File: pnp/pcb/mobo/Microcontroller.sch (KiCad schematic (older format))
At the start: 31 parts

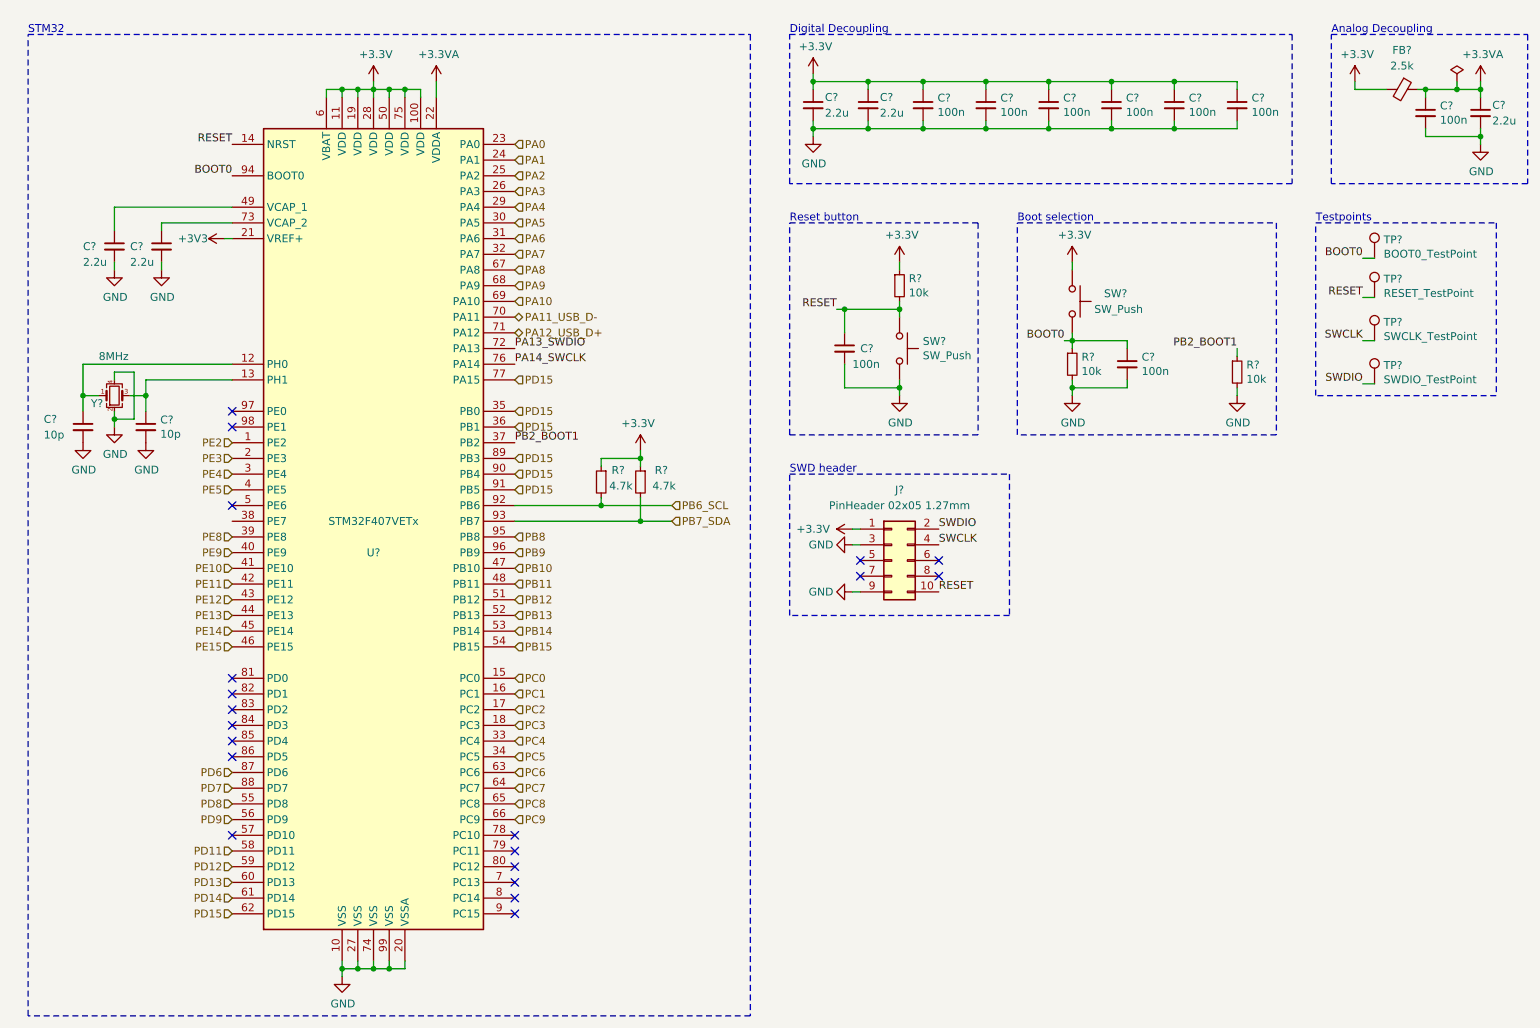
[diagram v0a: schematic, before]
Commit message: Schematic improvements
Ready for review @G-Pereira

No changes to PCB were made.

All symbol fields are not checked against the original symbols.
If wanted, an Index admin could restore this using the REV003 commit.
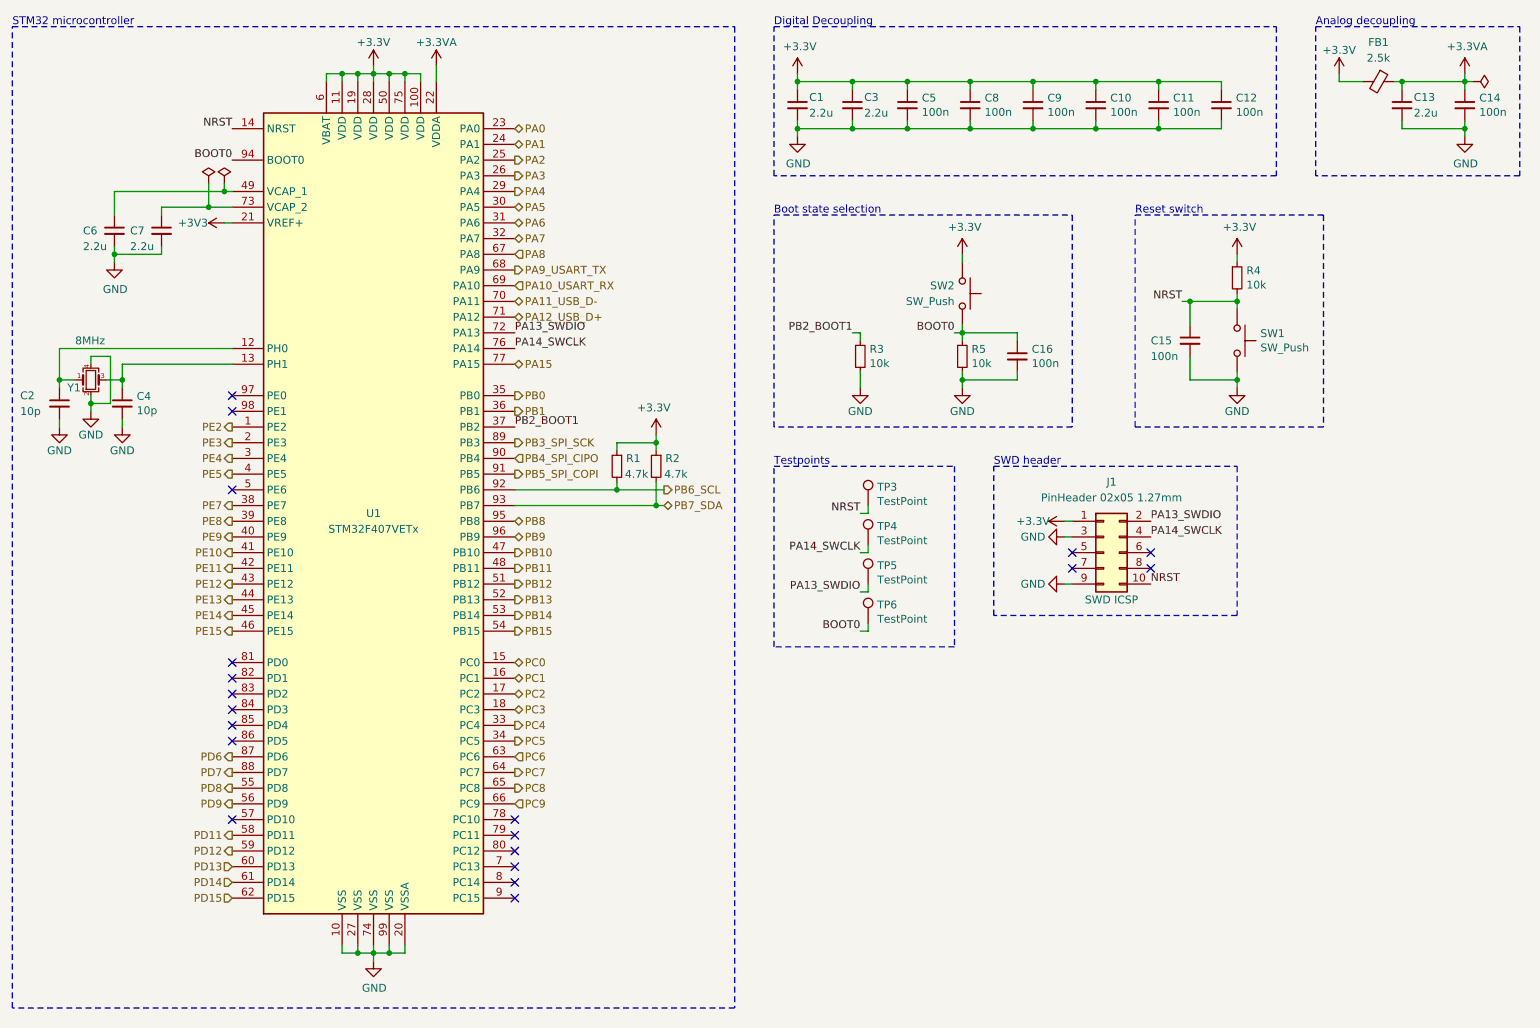
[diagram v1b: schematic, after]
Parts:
- removed C? (x2): 10p, Capacitor_SMD:C_0805_2012Metric, symbol Device:C_Small
- removed C? (x5): 2.2u, Capacitor_SMD:C_0805_2012Metric, symbol Device:C_Small
- removed C? (x9): 100n, Capacitor_SMD:C_0805_2012Metric, symbol Device:C_Small
- removed FB?: 2.5k, Inductor_SMD:L_0805_2012Metric, symbol Device:Ferrite_Bead_Small
- removed J?: PinHeader 02x05 1.27mm, symbol Connector_Generic:Conn_02x05_Odd_Even
- removed R? (x2): 4.7k, Resistor_SMD:R_0805_2012Metric, symbol Device:R_Small
- removed R? (x3): 10k, Resistor_SMD:R_0805_2012Metric, symbol Device:R_Small
- removed SW? (x2): SW_Push, Button_Switch_SMD:SW_SPST_B3S-1000, symbol Switch:SW_Push
- removed TP?: BOOT0_TestPoint, TestPoint:TestPoint_Pad_D2.0mm, symbol Connector:TestPoint
- removed TP?: RESET_TestPoint, TestPoint:TestPoint_Pad_D2.0mm, symbol Connector:TestPoint
- removed TP?: SWCLK_TestPoint, TestPoint:TestPoint_Pad_D2.0mm, symbol Connector:TestPoint
- removed TP?: SWDIO_TestPoint, TestPoint:TestPoint_Pad_D2.0mm, symbol Connector:TestPoint
- removed U?: STM32F407VETx, Package_QFP:LQFP-100_14x14mm_P0.5mm, symbol MCU_ST_STM32F4:STM32F407VETx
- removed Y?: 8MHz, Crystal:Crystal_SMD_3225-4Pin_3.2x2.5mm, symbol Device:Crystal_GND24_Small
- added C1, C13, C3, C6, C7: 2.2u, Capacitor_SMD:C_0805_2012Metric, symbol Device:C_Small
- added C10, C11, C12, C14, C15, C16, C5, C8, C9: 100n, Capacitor_SMD:C_0805_2012Metric, symbol Device:C_Small
- added C2, C4: 10p, Capacitor_SMD:C_0805_2012Metric, symbol Device:C_Small
- added FB1: 2.5k, Inductor_SMD:L_0805_2012Metric, symbol Device:Ferrite_Bead_Small
- added J1: PinHeader 02x05 1.27mm, Connector_PinHeader_1.27mm:PinHeader_2x05_P1.27mm_Vertical_SMD, symbol Connector_Generic:Conn_02x05_Odd_Even
- added R1, R2: 4.7k, Resistor_SMD:R_0805_2012Metric, symbol Device:R_Small
- added R3, R4, R5: 10k, Resistor_SMD:R_0805_2012Metric, symbol Device:R_Small
- added SW1, SW2: SW_Push, Button_Switch_SMD:SW_SPST_B3S-1000, symbol Switch:SW_Push
- added TP3, TP4, TP5, TP6: TestPoint, TestPoint:TestPoint_Pad_D2.0mm, symbol Connector:TestPoint
- added U1: STM32F407VETx, Package_QFP:LQFP-100_14x14mm_P0.5mm, symbol MCU_ST_STM32F4:STM32F407VETx
- added Y1: 8MHz, Crystal:Crystal_SMD_3225-4Pin_3.2x2.5mm, symbol Device:Crystal_GND24_Small
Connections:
- net +3.3VA: now also C13.1, C14.1, FB1.1, U1.22 (VDDA)
- net +3V3: now also C1.1, C10.1, C11.1, C12.1, C3.1, C5.1, C8.1, C9.1, FB1.2, J1.1 (Pin_1), R1.1, R2.1, R4.1, SW2.2, U1.100 (VDD), U1.11 (VDD), U1.19 (VDD), U1.21 (VREF+), U1.28 (VDD), U1.50 (VDD), U1.6 (VBAT), U1.75 (VDD)
- net BOOT0: now also C16.1, R5.1, SW2.1, TP6.1, U1.94 (BOOT0)
- net GND: now also C1.2, C10.2, C11.2, C12.2, C13.2, C14.2, C15.2, C16.2, C2.2, C3.2, C4.2, C5.2, C6.2, C7.2, C8.2, C9.2, J1.3 (Pin_3), J1.9 (Pin_9), R3.2, R5.2, SW1.1, U1.10 (VSS), U1.20 (VSSA), U1.27 (VSS), U1.74 (VSS), U1.99 (VSS), Y1.2, Y1.4
- net PA0: now also U1.23 (PA0)
- net PA1: now also U1.24 (PA1)
- net PA11_USB_D-: now also U1.70 (PA11)
- net PA12_USB_D+: now also U1.71 (PA12)
- net PA13_SWDIO: now also J1.2 (Pin_2), TP5.1, U1.72 (PA13)
- net PA14_SWCLK: now also J1.4 (Pin_4), TP4.1, U1.76 (PA14)
- net PA2: now also U1.25 (PA2)
- net PA3: now also U1.26 (PA3)
- net PA4: now also U1.29 (PA4)
- net PA5: now also U1.30 (PA5)
- net PA6: now also U1.31 (PA6)
- net PA7: now also U1.32 (PA7)
- net PA8: now also U1.67 (PA8)
- net PB10: now also U1.47 (PB10)
- net PB11: now also U1.48 (PB11)
- net PB12: now also U1.51 (PB12)
- net PB13: now also U1.52 (PB13)
- net PB14: now also U1.53 (PB14)
- net PB15: now also U1.54 (PB15)
- net PB2_BOOT1: now also R3.1, U1.37 (PB2)
- net PB6_SCL: now also R1.2, U1.92 (PB6)
- net PB7_SDA: now also R2.2, U1.93 (PB7)
- net PB8: now also U1.95 (PB8)
- net PB9: now also U1.96 (PB9)
- net PC0: now also U1.15 (PC0)
- net PC1: now also U1.16 (PC1)
- net PC2: now also U1.17 (PC2)
- net PC3: now also U1.18 (PC3)
- net PC4: now also U1.33 (PC4)
- net PC5: now also U1.34 (PC5)
- net PC6: now also U1.63 (PC6)
- net PC7: now also U1.64 (PC7)
- net PC8: now also U1.65 (PC8)
- net PC9: now also U1.66 (PC9)
- net PD11: now also U1.58 (PD11)
- net PD12: now also U1.59 (PD12)
- net PD13: now also U1.60 (PD13)
- net PD14: now also U1.61 (PD14)
- net PD15: now also U1.62 (PD15)
- net PD6: now also U1.87 (PD6)
- net PD7: now also U1.88 (PD7)
- net PD8: now also U1.55 (PD8)
- net PD9: now also U1.56 (PD9)
- net PE10: now also U1.41 (PE10)
- net PE11: now also U1.42 (PE11)
- net PE12: now also U1.43 (PE12)
- net PE13: now also U1.44 (PE13)
- net PE14: now also U1.45 (PE14)
- net PE15: now also U1.46 (PE15)
- net PE2: now also U1.1 (PE2)
- net PE3: now also U1.2 (PE3)
- net PE4: now also U1.3 (PE4)
- net PE5: now also U1.4 (PE5)
- net PE8: now also U1.39 (PE8)
- net PE9: now also U1.40 (PE9)
- new net: C4.1, U1.13 (PH1), Y1.3
- new net: C2.1, U1.12 (PH0), Y1.1
- new net: C6.1, U1.49 (VCAP_1)
- new net: C7.1, U1.73 (VCAP_2)
- new net NRST: C15.1, J1.10 (Pin_10), R4.2, SW1.2, TP3.1, U1.14 (NRST)
- new net PA10_USART_RX: U1.69 (PA10)
- new net PA15: U1.77 (PA15)
- new net PA9_USART_TX: U1.68 (PA9)
- new net PB0: U1.35 (PB0)
- new net PB1: U1.36 (PB1)
- new net PB3_SPI_SCK: U1.89 (PB3)
- new net PB4_SPI_CIPO: U1.90 (PB4)
- new net PB5_SPI_COPI: U1.91 (PB5)
- new net PE7: U1.38 (PE7)
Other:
- note added: "Analog decoupling"
- note added: "Boot state selection"
- note added: "Reset switch"
- note added: "STM32 microcontroller"
- note removed: "Analog Decoupling"
- note removed: "Boot selection"
- note removed: "Reset button"
- note removed: "STM32"
